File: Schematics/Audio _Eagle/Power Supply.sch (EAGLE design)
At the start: 43 parts, among them K1 G6RS, SW1 CT10-XXXX-A2

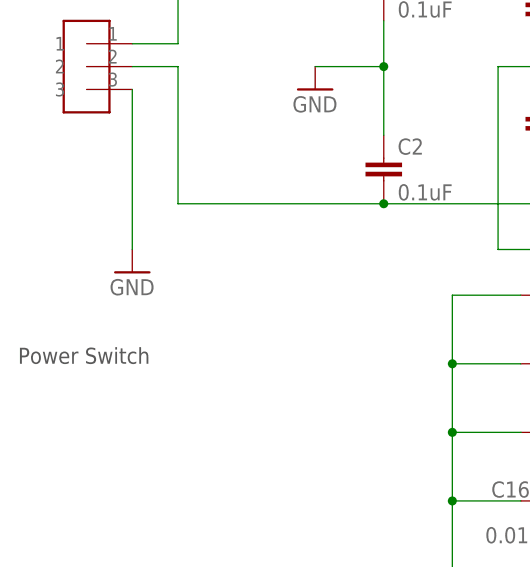
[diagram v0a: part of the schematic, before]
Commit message: Added documentation
Added data sheet for large caps, made rev 1 of power supply board, and
added project specific parts to a library.
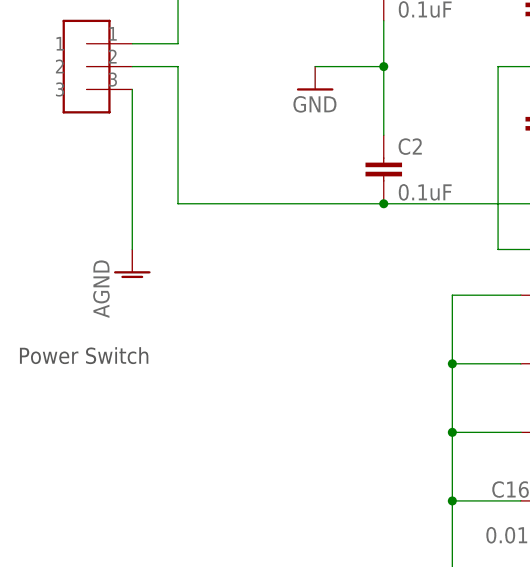
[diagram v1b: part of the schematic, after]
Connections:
- net AGND: now also U$1.3
- net GND: no longer U$1.3
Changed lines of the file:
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@@
 <setting verticaltext="up"/>
 </settings>
-<grid distance="0.05" unitdist="inch" unit="inch" style="lines" multiple="1" display="yes" altdistance="0.01" altunitdist="inch" altunit="inch"/>
+<grid distance="0.1" unitdist="inch" unit="inch" style="lines" multiple="1" display="no" altdistance="0.01" altunitdist="inch" altunit="inch"/>
 <layers>
 <layer number="1" name="Top" color="4" fill="1" visible="no" active="no"/>
@@
 <part name="AGND1" library="supply1" deviceset="AGND" device=""/>
 <part name="AGND2" library="supply1" deviceset="AGND" device=""/>
-<part name="GND3" library="supply1" deviceset="GND" device=""/>
 <part name="U$5" library="Headers" deviceset="1X2HEADER_100MIL" device=""/>
 <part name="SW1" library="switch-coto" deviceset="CT10-XXXX-" device="A2"/>
@@
 <part name="GND9" library="supply1" deviceset="GND" device=""/>
 <part name="GND10" library="supply1" deviceset="GND" device=""/>
+<part name="AGND3" library="supply1" deviceset="AGND" device=""/>
 </parts>
 <sheets>
@@
 <instance part="AGND1" gate="VR1" x="50.8" y="157.48"/>
 <instance part="AGND2" gate="VR1" x="96.52" y="111.76"/>
-<instance part="GND3" gate="1" x="17.78" y="96.52"/>
 <instance part="U$5" gate="G$1" x="81.28" y="172.72"/>
 <instance part="SW1" gate="G$1" x="104.14" y="175.26" rot="R90"/>
@@
 <instance part="GND9" gate="1" x="50.8" y="25.4"/>
 <instance part="GND10" gate="1" x="58.42" y="25.4"/>
+<instance part="AGND3" gate="VR1" x="17.78" y="96.52"/>
 </instances>
 <busses>
@@
 <wire x1="45.72" y1="119.38" x2="45.72" y2="111.76" width="0.1524" layer="91"/>
 <junction x="45.72" y="119.38"/>
-</segment>
-<segment>
-<pinref part="U$1" gate="G$1" pin="3"/>
-<wire x1="17.78" y1="116.84" x2="17.78" y2="99.06" width="0.1524" layer="91"/>
-<pinref part="GND3" gate="1" pin="GND"/>
 </segment>
 <segment>
@@
 <wire x1="167.64" y1="119.38" x2="198.12" y2="119.38" width="0.1524" layer="91"/>
 </segment>
-</net>
+<segment>
+<pinref part="U$1" gate="G$1" pin="3"/>
+<wire x1="17.78" y1="116.84" x2="17.78" y2="99.06" width="0.1524" layer="91"/>
+<pinref part="AGND3" gate="VR1" pin="AGND"/>
+</segment>
+</net>
